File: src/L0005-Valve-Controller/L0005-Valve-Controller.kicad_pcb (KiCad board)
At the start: 4 copper layers, 141.7 x 50.5 mm, 103 parts, among them J1 Jumper_NO, K1 AQH0223AX, K2 AQH0223AX, K3 AQH0223AX, K4 AQH0223AX, K5 AQH0223AX, K6 AQH0223AX, P1 3220-20-0200-00, P10 353620650, P11 353620650, P12 353620650, P13 353620650, P14 647676-3, P15 647676-3, P16 647676-2, P2 140-504-415-000, P3 647676-3, P4 647676-3, P5 647676-3, P6 647676-3, P7 647676-3, P8 647676-3, P9 647676-2, Q1 CMLDM7003, Q2 CMLDM7003, U1 STM32H750VBTx, U2 LMS8117AMP-3.3_NOPB, U3 MAX3370EXK+T, U4 MAX3370EXK+T, U5 Optocoupler

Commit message: routed rev 2
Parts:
- TP2, TP3, TP4, TP5: moved to B.Cu
- moved H3 111.7 mm to (61.2, 123.2)
- moved P9 88.7 mm to (122.6, 112.6)
- moved P16 87.1 mm to (132.9, 112.5)
- moved R22 84.9 mm to (149.4, 114.0), turned to 180 degrees
- moved C5 80.5 mm to (142.6, 101.8)
- moved D2 80.2 mm to (144.0, 115.6)
- moved P15 77.5 mm to (175.6, 100.6), turned to 90 degrees
- moved C8 75.5 mm to (127.2, 103.5)
- moved C11 72.7 mm to (139.6, 102.7), turned to 90 degrees
- moved TP2 71.7 mm to (124.1, 80.9), turned to 180 degrees
- moved U5 69.5 mm to (148.6, 109.8)
- moved C4 67.5 mm to (127.2, 101.6)
- moved H2 67.5 mm to (186.3, 122.9)
- moved C13 67.1 mm to (146.3, 87.2), turned to 180 degrees
- moved C12 66.1 mm to (137.6, 102.7), turned to 90 degrees
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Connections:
- C11 pad 1: Net-(C11-Pad1) -> Earth
- C12 pad 1: Net-(C11-Pad1) -> Earth
- C13 pad 1: Net-(C11-Pad1) -> Earth
- C14 pad 1: Net-(C11-Pad1) -> Earth
- U1 pad 60: unconnected-(U1-Pad60) -> EXECPT
- U1 pad 68: RX -> unconnected-(U1-Pad68)
- U1 pad 69: TX -> unconnected-(U1-Pad69)
- U1 pad 78: EXECPT -> TX
- U1 pad 79: unconnected-(U1-Pad79) -> RX
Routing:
- net SOL1: track 0.00 -> 87.3 mm, vias 0 -> 2
- net SOL4: track 0.00 -> 86.6 mm, vias 0 -> 4
- net AC_NEUTRAL: track 308.9 -> 223.6 mm, vias 8 -> 6
- net SOL3: track 0.00 -> 74.3 mm, vias 0 -> 2
- net SOL6: track 0.00 -> 72.3 mm, vias 0 -> 2
- net SBV2_PUL: track 5.66 -> 62.7 mm, vias 1 -> 2
- net Net-(K5-Pad2): track 63.7 -> 14.7 mm, vias 3 -> 0
- net Net-(C21-Pad2): track 35.0 -> 81.4 mm, vias 0 -> 2
- net Net-(K4-Pad2): track 52.9 -> 8.43 mm, vias 3 -> 0
- net SBV1_PUL: track 4.98 -> 42.7 mm, vias 0 -> 2
- net SOL5: track 3.28 -> 39.7 mm, vias 0 -> 2
- net SOL2: track 0.00 -> 32.6 mm
- net SBV2_EN: track 12.0 -> 43.9 mm, vias 1 -> 2
- net Net-(P12-Pad2): track 40.6 -> 9.69 mm, vias 2 -> 0
- net Net-(P11-Pad2): track 35.7 -> 5.62 mm
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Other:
- board size 141.7 x 50.5 mm -> 134.2 x 60.2 mm
- board text added: "L0005 Revision 2.0"
- board text removed: "L0005 Revision 1.0"

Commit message: fixed 3D model paths
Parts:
- B1: value PTS647SM38SMTR2LFS -> SW_PTS647SM38SMTR2LFS_CNK

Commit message: added 3D model for rev 2.0
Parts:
- B1: value SW_PTS647SM38SMTR2LFS_CNK -> PTS647SM38SMTR2LFS

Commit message: routed rev3
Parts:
- removed C24, C25: 0.1uF, L0005-Valve-Controller:CAP_0603
- removed TP1: TP, L0005-Valve-Controller:TP
- removed U4: MAX3370EXK+T, L0005-Valve-Controller:MAX3370EXK&plus_T
- added J2: Jumper_NO, L0005-Valve-Controller:Jumper-NO, F.Cu at (113.5, 103.8)
- added P17: USB, L0005-Valve-Controller:USB-TypeB, F.Cu at (177.6, 92.6)
- added Q3: CMLDM7003, L0005-Valve-Controller:CMLDM7003 TR, F.Cu at (159.0, 113.0)
- added R28: 280, L0005-Valve-Controller:RES_0603, F.Cu at (148.7, 101.9)
- added R29: 10k, L0005-Valve-Controller:RES_0603, F.Cu at (183.1, 82.8)
- added R30: 4.7k, L0005-Valve-Controller:RES_0603, F.Cu at (158.6, 87.5)
- added R31: 10k, L0005-Valve-Controller:RES_0603, F.Cu at (158.6, 90.2)
- added R32: 20k, L0005-Valve-Controller:RES_0603, F.Cu at (183.1, 80.6)
- C22: value 0.1uF -> 1uF
- D3: value LED_AMBER -> CLMVC-FKA-CL1D1L71BB7C3C3; footprint L0005-Valve-Controller:150120AS75000 -> L0005-Valve-Controller:CLMVC-FKA-CL1D1L71BB7C3C3
- D4: value LED_RED -> SP0504BAHTG; footprint L0005-Valve-Controller:LED_RED -> L0005-Valve-Controller:SP0504BAHTG
- R24: value 240 -> 68
- R25: value 240 -> 82
- U3: value MAX3370EXK+T -> CP2102-GMR(QFN28); footprint L0005-Valve-Controller:MAX3370EXK&plus_T -> L0005-Valve-Controller:CP2012-GMR
- moved C22 26.7 mm to (165.2, 92.2), turned to 0 degrees
- moved P15 24.6 mm to (161.0, 80.7), turned to 180 degrees
- moved D3 23.8 mm to (152.3, 100.3), turned to 0 degrees
- moved R24 23.7 mm to (156.3, 102.2), turned to 90 degrees
- moved C23 21.6 mm to (165.1, 90.3), turned to 0 degrees
- moved D4 21.3 mm to (169.3, 96.6), turned to 0 degrees
- moved U3 20.3 mm to (160.2, 95.1), turned to 180 degrees
- moved LOGO1 18.1 mm to (165.0, 104.8)
- moved R17 12.9 mm to (180.5, 104.4)
- moved R20 12.9 mm to (175.7, 104.4)
- moved R21 12.9 mm to (182.4, 104.3)
- moved R15 12.9 mm to (177.5, 104.4)
- moved R25 11.2 mm to (151.8, 104.6)
- moved D1 9.82 mm to (144.1, 79.1)
- moved R1 9.82 mm to (139.4, 79.1)
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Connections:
- B1 pad 3: Earth -> Net-(J2-B)
- C22 pad 1: Earth -> 5V
- C22 pad 2: 3.3V -> Earth
- C23 pad 1: Earth -> 5V
- C23 pad 2: 3.3V -> Earth
- D3 pad 1: Net-(D3-Pad1) -> 3.3V
- D3 pad 2: STATUS -> Net-(D3-Pad2)
- D4 pad 1: Net-(D4-Pad1) -> /Power/D-
- D4 pad 2: EXECPT -> Earth
- P10 pad 2: Net-(P10-Pad2) -> SBV1_DIR-
- P10 pad 4: Net-(P10-Pad4) -> SBV1_EN-
- P10 pad 5: /Valves/SBV1_PUL5 -> 5V
- P10 pad 6: Earth -> SBV1_PUL-
- P12 pad 2: Net-(P12-Pad2) -> SBV2_DIR-
- P12 pad 4: Net-(P12-Pad4) -> SBV2_EN-
- P12 pad 5: /Valves/SBV2_PUL5 -> 5V
- P12 pad 6: Earth -> SBV2_PUL-
- Q1 pad 3: Net-(P10-Pad2) -> SBV1_EN-
- Q1 pad 6: Net-(P10-Pad4) -> SBV1_DIR-
- Q2 pad 3: Net-(P12-Pad2) -> SBV2_EN-
- Q2 pad 6: Net-(P12-Pad4) -> SBV2_DIR-
- R24 pad 1: Net-(D3-Pad1) -> STATUS_B
- R24 pad 2: Earth -> Net-(D3-Pad2)
- R25 pad 1: Net-(D4-Pad1) -> STATUS_G
- R25 pad 2: Earth -> Net-(D3-Pad3)
- U1 pad 25: unconnected-(U1-Pad25) -> SBV2_PUL
- U1 pad 5: SBV2_PUL -> unconnected-(U1-PE6-Pad5)
- U1 pad 53: unconnected-(U1-Pad53) -> RX_USB
- U1 pad 54: unconnected-(U1-Pad54) -> TX_USB
- U1 pad 55: unconnected-(U1-Pad55) -> STATUS_G
- U1 pad 56: unconnected-(U1-Pad56) -> STATUS_R
- U1 pad 57: unconnected-(U1-Pad57) -> STATUS_B
- U1 pad 58: unconnected-(U1-Pad58) -> ~{USB_SUSPEND}
- U1 pad 59: unconnected-(U1-Pad59) -> ~{USB_RST}
- U1 pad 60: EXECPT -> USB_DETECT
- U1 pad 61: unconnected-(U1-Pad61) -> ENCD2_A
- U1 pad 63: ENCD2_A -> unconnected-(U1-PC6-Pad63)
- U1 pad 77: STATUS -> unconnected-(U1-PA15-Pad77)
- U3 pad 1: 3.3V -> unconnected-(U3-DCD-Pad1)
- U3 pad 2: Earth -> unconnected-(U3-RI-Pad2)
- U3 pad 3: SBV1_PUL -> Earth
- U3 pad 4: /Valves/SBV1_PUL5 -> /Power/D+
- U3 pad 5: 5V -> /Power/D-
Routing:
- net USB_DETECT: track 0.00 -> 45.7 mm
- net 5V: track 186.6 -> 220.4 mm, vias 1 -> 0
- net TX_USB: track 0.00 -> 24.6 mm, vias 0 -> 2
- net Net-(P10-Pad4): track 24.5 -> 0.00 mm, vias 2 -> 0
- net ~{USB_RST}: track 0.00 -> 24.4 mm
- net SBV2_PUL: track 62.7 -> 39.0 mm
- net Earth: track 149.9 -> 126.2 mm, vias 22 -> 25
- net RX_USB: track 0.00 -> 23.6 mm, vias 0 -> 2
- net SBV2_PUL-: track 0.00 -> 21.3 mm
- net ~{USB_SUSPEND}: track 0.00 -> 20.6 mm
- net STATUS_B: track 0.00 -> 20.0 mm
- net SBV1_PUL-: track 0.00 -> 18.8 mm
- net PG2: track 54.2 -> 35.6 mm
- net Net-(P12-Pad4): track 18.1 -> 0.00 mm
- net STATUS_G: track 0.00 -> 17.7 mm
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- added copper zone on B.Cu, net Earth
- added copper zone on F.Cu, net Earth
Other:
- board text added: "L0005 Valve Controller Revision 3.0"
- board text removed: "EXCEPT"
- board text removed: "L0005 Revision 2.0"

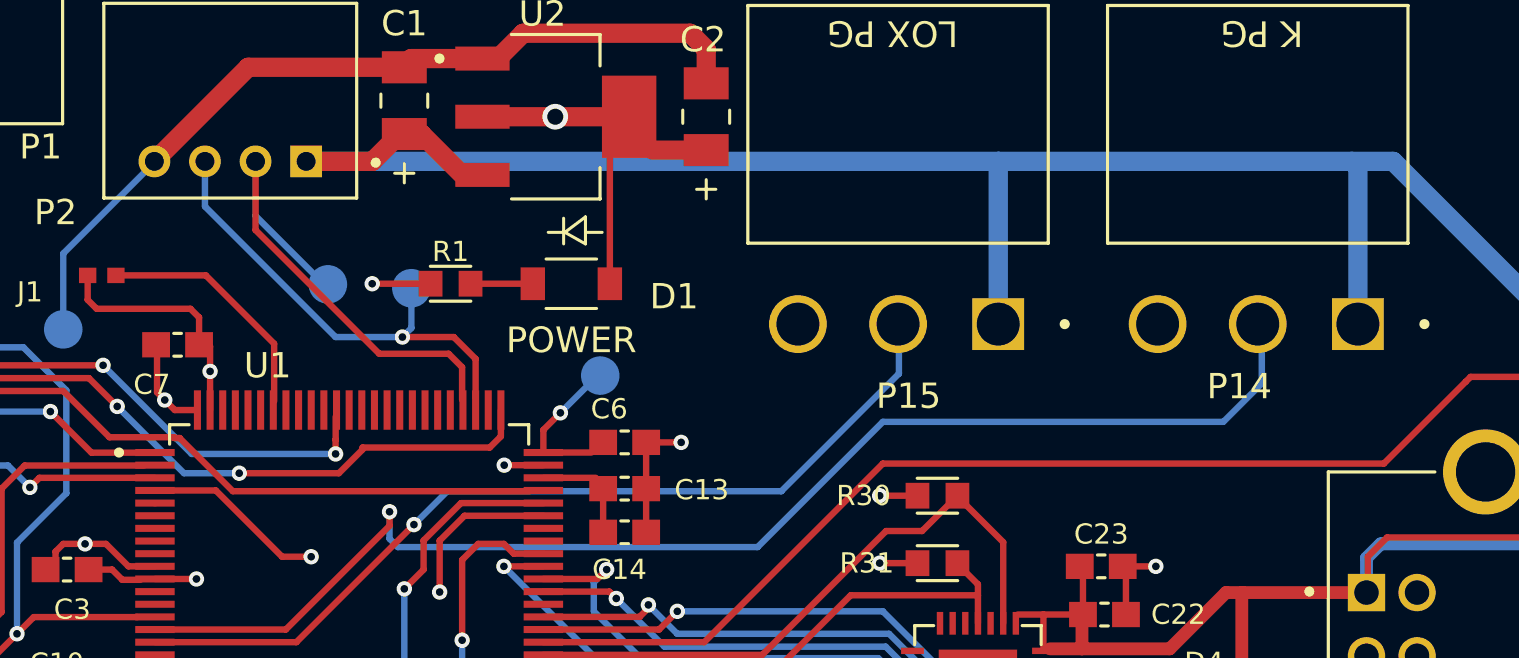
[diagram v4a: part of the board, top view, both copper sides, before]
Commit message: fixed photogate pinouts to allow for straight cable to photogate connector
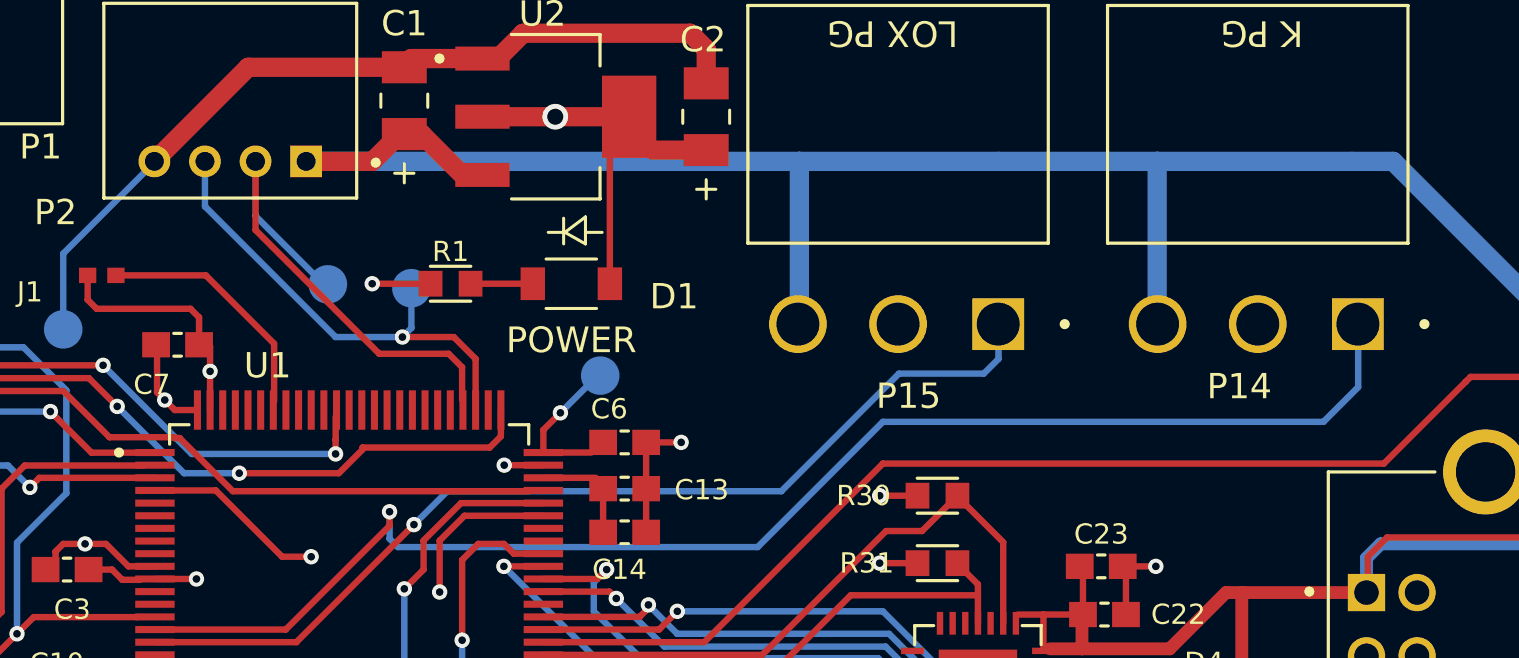
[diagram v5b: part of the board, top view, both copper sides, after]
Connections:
- P14 pad 1: 5V -> PG1
- P14 pad 2: PG1 -> Earth
- P14 pad 3: Earth -> 5V
- P15 pad 1: 5V -> PG2
- P15 pad 2: PG2 -> Earth
- P15 pad 3: Earth -> 5V
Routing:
- net PG1: track 52.2 -> 56.1 mm
- net PG2: track 35.6 -> 39.2 mm
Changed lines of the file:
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@@
       (drillshape 0)
       (scaleselection 1)
-      (outputdirectory "../../production/")
+      (outputdirectory "../../production/gerbers/")
     )
   )
@@
       (stroke (width 0.2) (type solid)) (fill none) (layer "F.Fab"))
     (pad "1" thru_hole rect (at 0 0 180) (size 2.05 2.05) (drill 1.7) (layers "*.Cu" "*.Mask")
-      (net 6 "5V") (pinfunction "1") (pintype "passive"))
+      (net 81 "PG1") (pinfunction "1") (pintype "passive"))
     (pad "2" thru_hole circle (at 3.96 0 180) (size 2.286 2.286) (drill 1.7) (layers "*.Cu" "*.Mask")
-      (net 81 "PG1") (pinfunction "2") (pintype "passive"))
+      (net 3 "Earth") (pinfunction "2") (pintype "passive"))
     (pad "3" thru_hole circle (at 7.92 0 180) (size 2.286 2.286) (drill 1.7) (layers "*.Cu" "*.Mask")
-      (net 3 "Earth") (pinfunction "3") (pintype "passive"))
+      (net 6 "5V") (pinfunction "3") (pintype "passive"))
     (model "/home/olsport/Documents/SDR/PCB/Valve-Controller/CAD/3Dfiles/647676-3.stp"
       (offset (xyz 3.81 -12.7 5.08))
@@
       (stroke (width 0.2) (type solid)) (fill none) (layer "F.Fab"))
     (pad "1" thru_hole rect (at 0 0 180) (size 2.05 2.05) (drill 1.7) (layers "*.Cu" "*.Mask")
-      (net 6 "5V") (pinfunction "1") (pintype "passive"))
+      (net 82 "PG2") (pinfunction "1") (pintype "passive"))
     (pad "2" thru_hole circle (at 3.96 0 180) (size 2.286 2.286) (drill 1.7) (layers "*.Cu" "*.Mask")
-      (net 82 "PG2") (pinfunction "2") (pintype "passive"))
+      (net 3 "Earth") (pinfunction "2") (pintype "passive"))
     (pad "3" thru_hole circle (at 7.92 0 180) (size 2.286 2.286) (drill 1.7) (layers "*.Cu" "*.Mask")
-      (net 3 "Earth") (pinfunction "3") (pintype "passive"))
+      (net 6 "5V") (pinfunction "3") (pintype "passive"))
     (model "/home/olsport/Documents/SDR/PCB/Valve-Controller/CAD/3Dfiles/647676-3.stp"
       (offset (xyz 3.81 -12.7 5.08))
@@
   (segment (start 183.924 87.729) (end 182.499 89.154) (width 0.254) (layer "F.Cu") (net 6))
   (segment (start 177.9016 118.4176) (end 179.9816 118.4176) (width 0.762) (layer "B.Cu") (net 6))
-  (segment (start 175.2495 74.5255) (end 175.006 74.282) (width 0.762) (layer "B.Cu") (net 6))
-  (segment (start 161.0255 74.2925) (end 161.036 74.282) (width 0.762) (layer "B.Cu") (net 6))
+  (segment (start 167.3098 74.282) (end 167.3098 80.772) (width 0.762) (layer "B.Cu") (net 6))
   (segment (start 177.9308 110.4176) (end 180.0352 112.522) (width 0.762) (layer "B.Cu") (net 6))
   (segment (start 176.149 89.408) (end 187.0424 89.408) (width 0.508) (layer "B.Cu") (net 6))
-  (segment (start 161.0255 80.7175) (end 161.0255 74.2925) (width 0.762) (layer "B.Cu") (net 6))
   (segment (start 175.5885 89.9685) (end 176.149 89.408) (width 0.508) (layer "B.Cu") (net 6))
-  (segment (start 161.036 74.282) (end 175.006 74.282) (width 0.762) (layer "B.Cu") (net 6))
+  (segment (start 161.036 74.282) (end 167.3098 74.282) (width 0.762) (layer "B.Cu") (net 6))
+  (segment (start 167.3098 74.282) (end 175.006 74.282) (width 0.762) (layer "B.Cu") (net 6))
   (segment (start 180.0352 118.364) (end 180.0352 121.5644) (width 0.762) (layer "B.Cu") (net 6))
+  (segment (start 153.162 74.282) (end 153.162 80.9244) (width 0.762) (layer "B.Cu") (net 6))
   (segment (start 186.0296 106.5276) (end 186.8932 106.5276) (width 0.762) (layer "B.Cu") (net 6))
   (segment (start 176.644 74.282) (end 187.0424 84.6804) (width 0.762) (layer "B.Cu") (net 6))
   (segment (start 175.006 74.282) (end 176.644 74.282) (width 0.762) (layer "B.Cu") (net 6))
+  (segment (start 153.162 74.282) (end 161.036 74.282) (width 0.762) (layer "B.Cu") (net 6))
   (segment (start 180.0352 114.427) (end 180.0352 118.364) (width 0.762) (layer "B.Cu") (net 6))
   (segment (start 179.9816 118.4176) (end 180.0352 118.364) (width 0.762) (layer "B.Cu") (net 6))
   (segment (start 180.0352 114.427) (end 177.8 114.427) (width 0.762) (layer "B.Cu") (net 6))
   (segment (start 180.0352 112.522) (end 180.0352 114.427) (width 0.762) (layer "B.Cu") (net 6))
-  (segment (start 175.2495 80.7175) (end 175.2495 74.5255) (width 0.762) (layer "B.Cu") (net 6))
   (segment (start 187.0424 84.6804) (end 187.0424 89.408) (width 0.762) (layer "B.Cu") (net 6))
   (segment (start 177.9016 110.4176) (end 177.9308 110.4176) (width 0.762) (layer "B.Cu") (net 6))
+  (segment (start 133.6576 74.282) (end 153.162 74.282) (width 0.762) (layer "B.Cu") (net 6))
   (segment (start 180.0352 112.522) (end 186.0296 106.5276) (width 0.762) (layer "B.Cu") (net 6))
   (segment (start 187.0424 89.408) (end 187.0424 106.5075) (width 0.762) (layer "B.Cu") (net 6))
   (segment (start 175.5885 91.333) (end 175.5885 89.9685) (width 0.508) (layer "B.Cu") (net 6))
-  (segment (start 133.6576 74.282) (end 161.036 74.282) (width 0.762) (layer "B.Cu") (net 6))
   (segment (start 178.816 122.7836) (end 170.0276 122.7836) (width 0.762) (layer "B.Cu") (net 6))
   (segment (start 180.0352 121.5644) (end 178.816 122.7836) (width 0.762) (layer "B.Cu") (net 6))
@@
   (segment (start 136.9568 88.69312) (end 136.9568 88.138) (width 0.254) (layer "F.Cu") (net 81))
   (via (at 136.9568 88.138) (size 0.60706) (drill 0.30226) (layers "F.Cu" "B.Cu") (net 81))
-  (segment (start 136.9568 89.2048) (end 137.287 89.535) (width 0.254) (layer "B.Cu") (net 81))
+  (segment (start 156.464 84.582) (end 173.8884 84.582) (width 0.254) (layer "B.Cu") (net 81))
   (segment (start 137.287 89.535) (end 151.511 89.535) (width 0.254) (layer "B.Cu") (net 81))
-  (segment (start 169.926 84.582) (end 171.45 83.058) (width 0.254) (layer "B.Cu") (net 81))
-  (segment (start 151.511 89.535) (end 156.464 84.582) (width 0.254) (layer "B.Cu") (net 81))
+  (segment (start 136.9568 89.2048) (end 137.287 89.535) (width 0.254) (layer "B.Cu") (net 81))
   (segment (start 136.9568 88.138) (end 136.9568 89.2048) (width 0.254) (layer "B.Cu") (net 81))
-  (segment (start 156.464 84.582) (end 169.926 84.582) (width 0.254) (layer "B.Cu") (net 81))
-  (segment (start 171.45 83.058) (end 171.45 80.772) (width 0.254) (layer "B.Cu") (net 81))
+  (segment (start 175.26 83.2104) (end 175.26 80.7466) (width 0.254) (layer "B.Cu") (net 81))
+  (segment (start 151.511 89.535) (end 156.464 84.582) (width 0.254) (layer "B.Cu") (net 81))
+  (segment (start 173.8884 84.582) (end 175.26 83.2104) (width 0.254) (layer "B.Cu") (net 81))
   (segment (start 133.2724 93.2956) (end 137.922 88.646) (width 0.254) (layer "F.Cu") (net 82))
   (segment (start 127.6797 93.2956) (end 133.2724 93.2956) (width 0.254) (layer "F.Cu") (net 82))
   (via (at 137.922 88.646) (size 0.60706) (drill 0.30226) (layers "F.Cu" "B.Cu") (net 82))
-  (segment (start 157.099 82.677) (end 157.099 80.899) (width 0.254) (layer "B.Cu") (net 82))
+  (segment (start 157.099 82.677) (end 160.4518 82.677) (width 0.254) (layer "B.Cu") (net 82))
   (segment (start 139.2428 87.3252) (end 152.4508 87.3252) (width 0.254) (layer "B.Cu") (net 82))
-  (segment (start 152.4508 87.3252) (end 157.099 82.677) (width 0.254) (layer "B.Cu") (net 82))
+  (segment (start 161.036 82.0928) (end 161.036 80.8482) (width 0.254) (layer "B.Cu") (net 82))
+  (segment (start 160.4518 82.677) (end 161.036 82.0928) (width 0.254) (layer "B.Cu") (net 82))
   (segment (start 137.922 88.646) (end 139.2428 87.3252) (width 0.254) (layer "B.Cu") (net 82))
+  (segment (start 152.4508 87.3252) (end 157.099 82.677) (width 0.254) (layer "B.Cu") (net 82))
   (segment (start 136.7764 108.3056) (end 134.7216 108.3056) (width 0.254) (layer "F.Cu") (net 83))
   (segment (start 134.7216 108.3056) (end 133.0452 109.982) (width 0.254) (layer "F.Cu") (net 83))
@@
   (segment (start 160.224 91.009) (end 159.766 90.551) (width 0.254) (layer "F.Cu") (net 108))
   (segment (start 160.224 92.549) (end 160.224 91.44) (width 0.254) (layer "F.Cu") (net 108))
-  (segment (start 127.6797 87.7956) (end 127.6797 87.8017) (width 0.254) (layer "F.Cu") (net 109))
   (segment (start 143.0397 96.2956) (end 147.2904 96.2956) (width 0.25) (layer "F.Cu") (net 139))
   (segment (start 160.724 100.399) (end 160.724 97.729) (width 0.25) (layer "F.Cu") (net 139))
